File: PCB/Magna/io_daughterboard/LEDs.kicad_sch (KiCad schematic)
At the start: 96 parts, among them U2001 74HC595, U2002 74HC595, U2003 74HC595, U2004 74HC595, U2005 74HC595

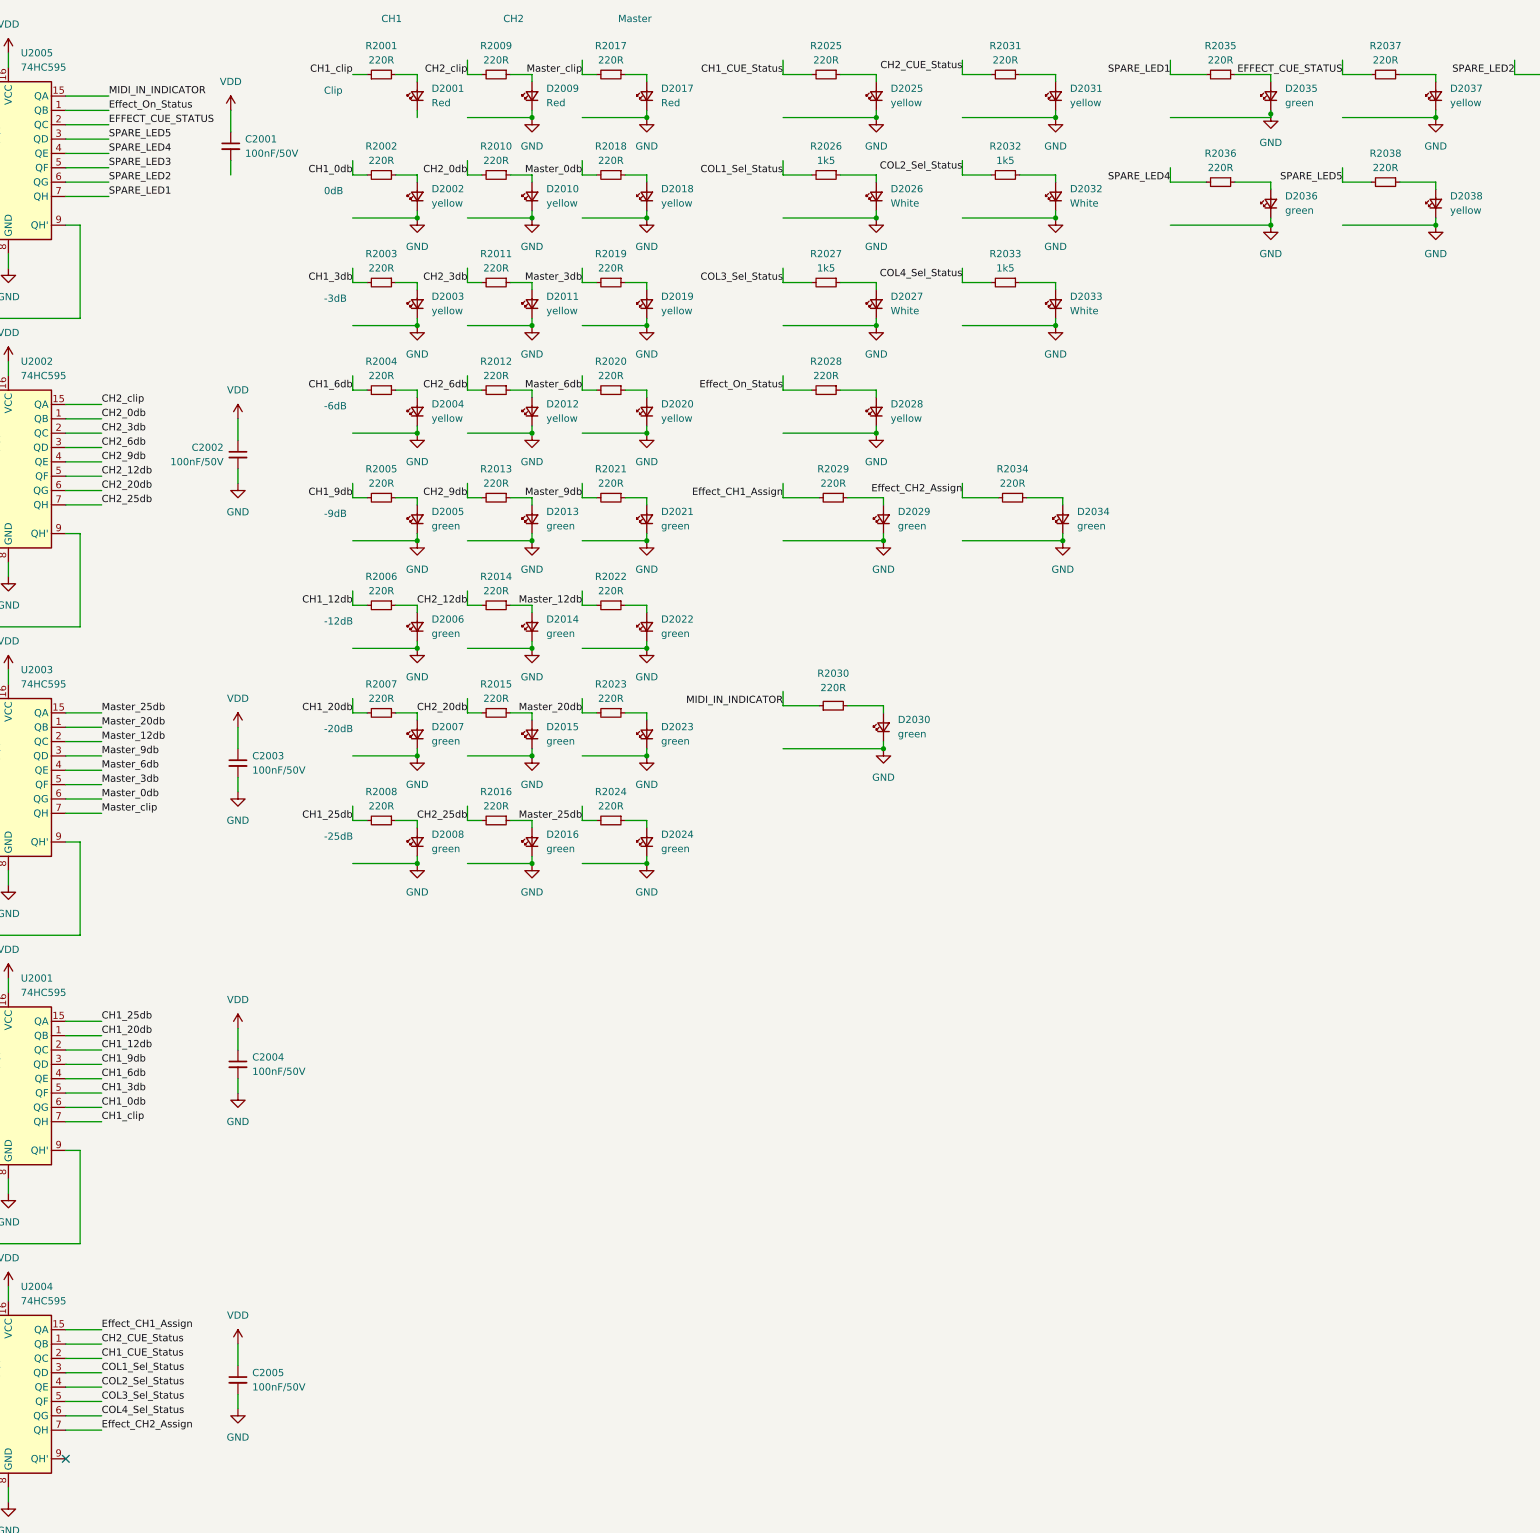
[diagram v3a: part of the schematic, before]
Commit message: Add more routing to IO Daugherboard
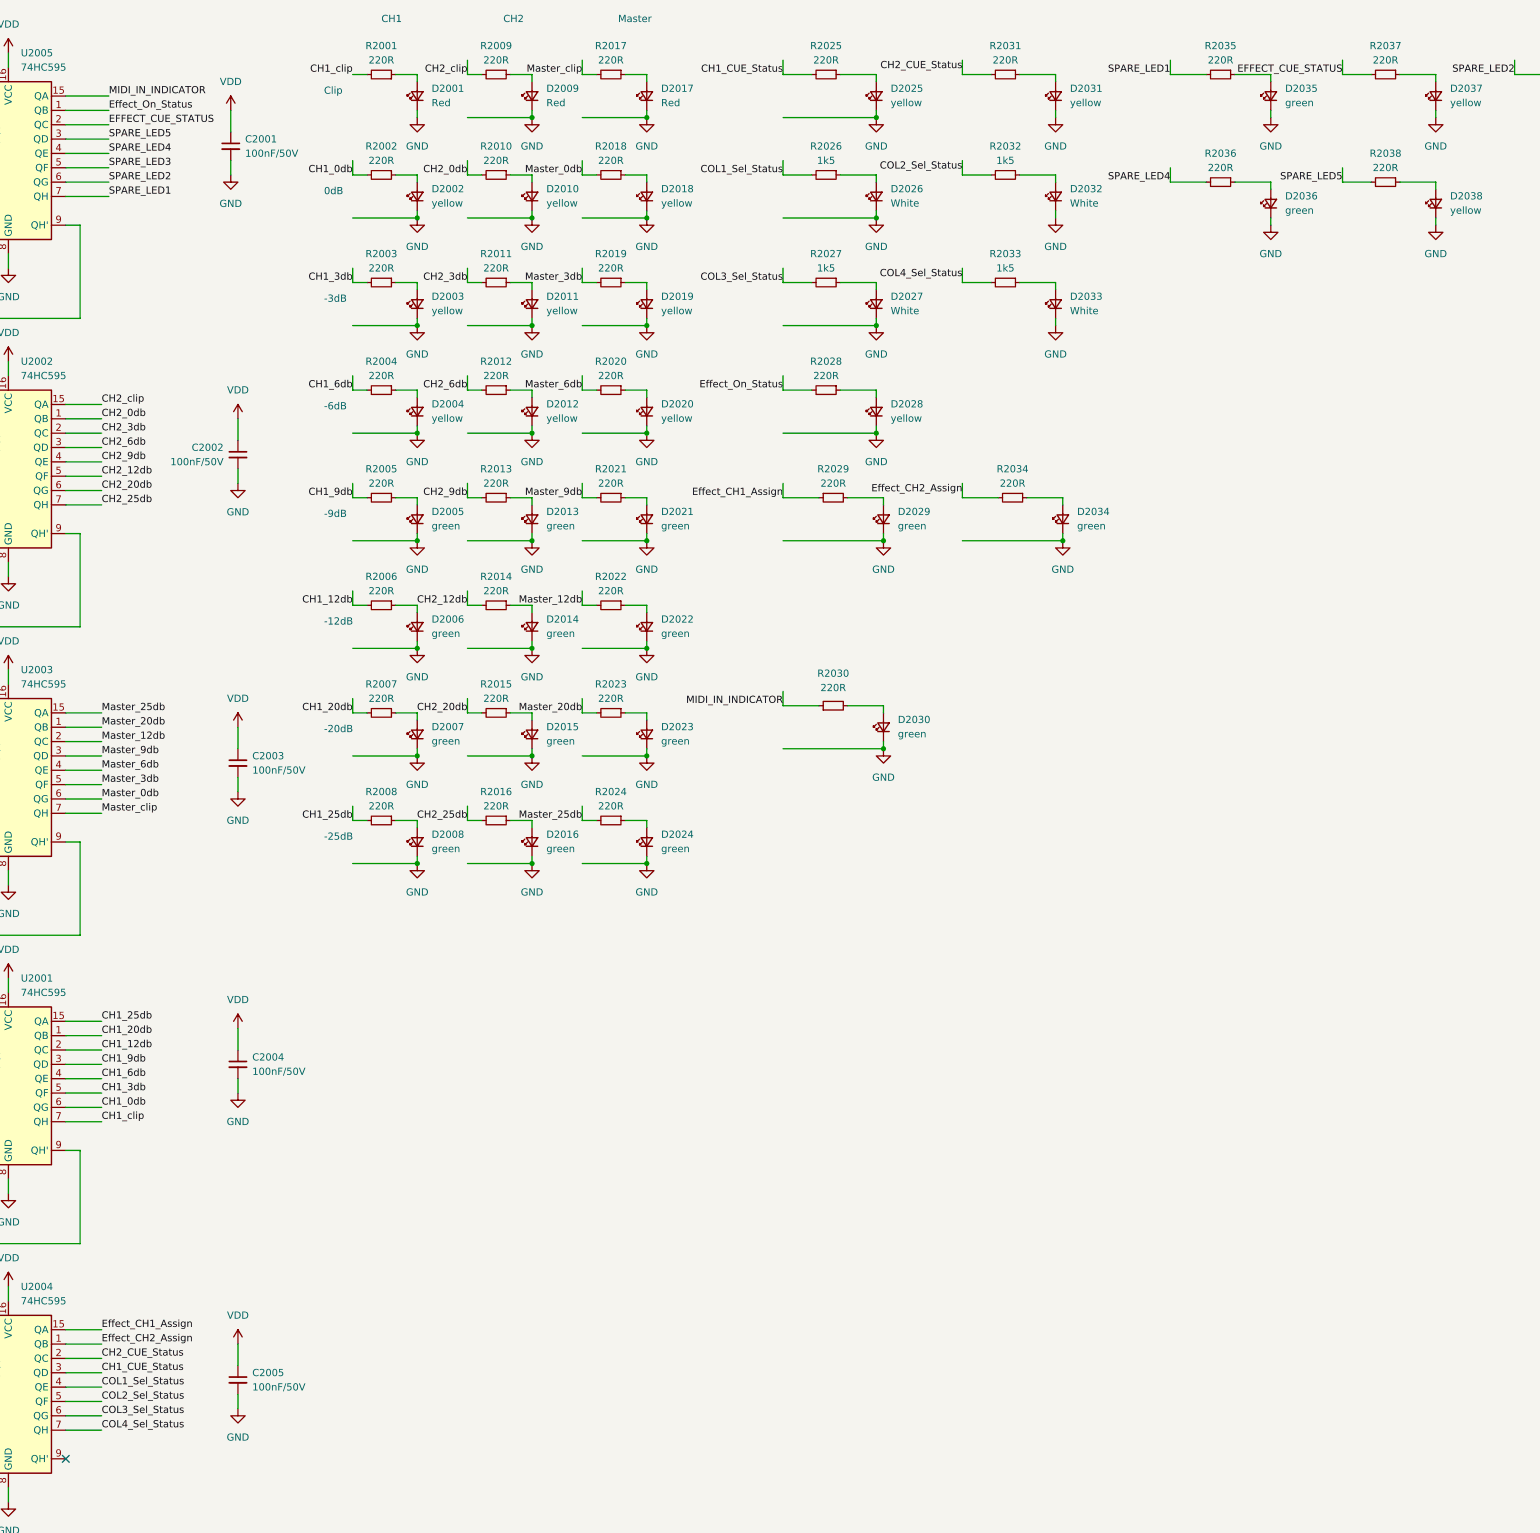
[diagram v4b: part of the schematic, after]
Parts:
- TP2001, TP2002, TP2003, TP2004, TP2005, TP2006: footprint TestPoint:TestPoint_Keystone_5005-5009_Compact -> TestPoint:TestPoint_Keystone_5000-5004_Miniature
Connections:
- net CH1_CUE_Status: now also U2004.3 (QD); no longer U2004.2 (QC)
- net CH1_clip: now also R2001.2; no longer R2001.1
- net CH2_CUE_Status: now also U2004.2 (QC); no longer U2004.1 (QB)
- net COL1_Sel_Status: now also U2004.4 (QE); no longer U2004.3 (QD)
- net COL2_Sel_Status: now also U2004.5 (QF); no longer U2004.4 (QE)
- net COL3_Sel_Status: now also U2004.6 (QG); no longer U2004.5 (QF)
- net COL4_Sel_Status: now also U2004.7 (QH); no longer U2004.6 (QG)
- net Effect_CH1_Assign: now also R2029.1; no longer R2029.2
- net Effect_CH2_Assign: now also U2004.1 (QB); no longer U2004.7 (QH)
- net GND: now also C2001.2, D2001.1 (K)
- net at D2001.2 (A): now also R2001.1; no longer R2001.2
- net at D2029.2 (A): now also R2029.2; no longer R2029.1
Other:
- moved on the sheet: R2001, R2029

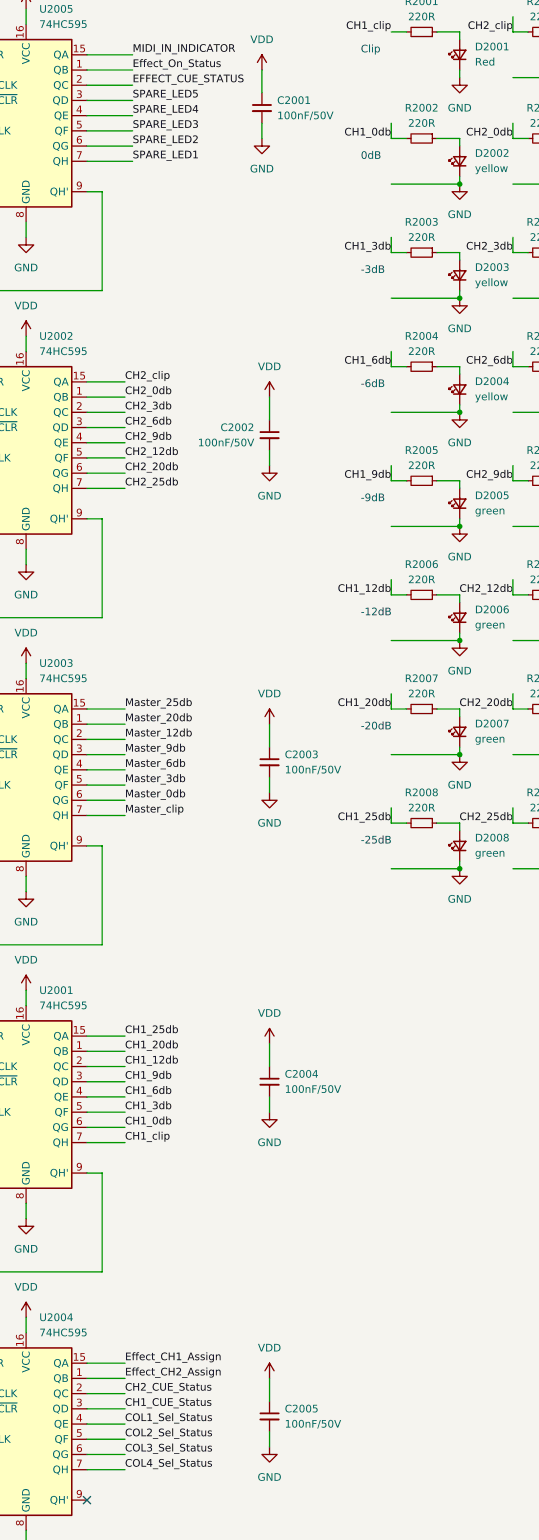
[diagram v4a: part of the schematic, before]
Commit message: Change all capacitors to 22uF on IO board(#5)
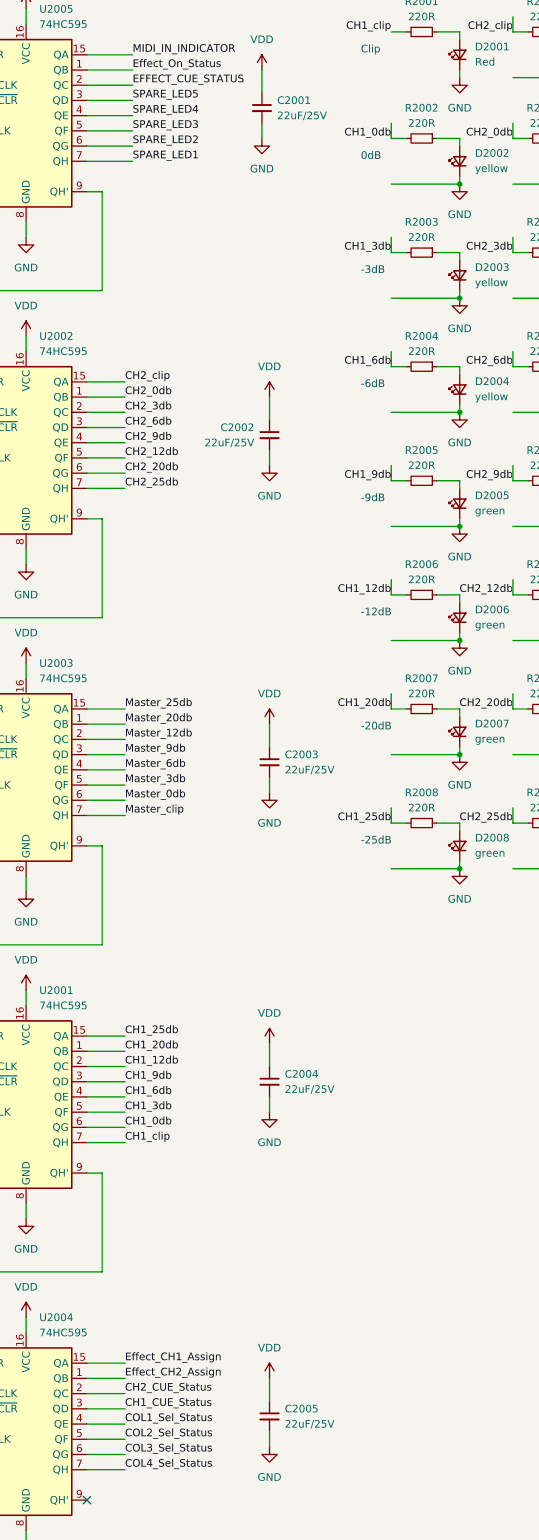
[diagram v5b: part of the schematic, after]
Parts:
- C2001, C2002, C2003, C2004, C2005: value 100nF/50V -> 22uF/25V; LCSC C49678 -> C45783
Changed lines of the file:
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@@
       (effects (font (size 1.27 1.27)) (justify right))
     )
-    (property "Value" "100nF/50V" (at 129.54 200.6663 0)
+    (property "Value" "22uF/25V" (at 129.54 200.6663 0)
       (effects (font (size 1.27 1.27)) (justify right))
     )
@@
       (effects (font (size 1.27 1.27)) hide)
     )
-    (property "LCSC" "C49678" (at 127 199.39 0)
+    (property "LCSC" "C45783" (at 127 199.39 0)
       (effects (font (size 1.27 1.27)) hide)
     )
@@
       (effects (font (size 1.27 1.27)) (justify right))
     )
-    (property "Value" "100nF/50V" (at 124.46 92.7163 0)
+    (property "Value" "22uF/25V" (at 124.46 92.7163 0)
       (effects (font (size 1.27 1.27)) (justify right))
     )
@@
       (effects (font (size 1.27 1.27)) hide)
     )
-    (property "LCSC" "C49678" (at 127 91.44 0)
+    (property "LCSC" "C45783" (at 127 91.44 0)
       (effects (font (size 1.27 1.27)) hide)
     )
@@
       (effects (font (size 1.27 1.27)) (justify right))
     )
-    (property "Value" "100nF/50V" (at 129.54 256.5463 0)
+    (property "Value" "22uF/25V" (at 129.54 256.5463 0)
       (effects (font (size 1.27 1.27)) (justify right))
     )
@@
       (effects (font (size 1.27 1.27)) hide)
     )
-    (property "LCSC" "C49678" (at 127 255.27 0)
+    (property "LCSC" "C45783" (at 127 255.27 0)
       (effects (font (size 1.27 1.27)) hide)
     )
@@
       (effects (font (size 1.27 1.27)) (justify right))
     )
-    (property "Value" "100nF/50V" (at 129.54 147.3263 0)
+    (property "Value" "22uF/25V" (at 129.54 147.3263 0)
       (effects (font (size 1.27 1.27)) (justify right))
     )
@@
       (effects (font (size 1.27 1.27)) hide)
     )
-    (property "LCSC" "C49678" (at 127 146.05 0)
+    (property "LCSC" "C45783" (at 127 146.05 0)
       (effects (font (size 1.27 1.27)) hide)
     )
@@
       (effects (font (size 1.27 1.27)) (justify right))
     )
-    (property "Value" "100nF/50V" (at 128.27 38.1063 0)
+    (property "Value" "22uF/25V" (at 128.27 38.1063 0)
       (effects (font (size 1.27 1.27)) (justify right))
     )
@@
       (effects (font (size 1.27 1.27)) hide)
     )
-    (property "LCSC" "C49678" (at 125.73 36.83 0)
-      (effects (font (size 1.27 1.27)) hide)
-    )
+    (property "LCSC" "C45783" (at 125.73 36.83 0)
+      (effects (font (size 1.27 1.27)) hide)
+    )
